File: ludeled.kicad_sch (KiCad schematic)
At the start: 2 parts

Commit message: Major layout and placement complete
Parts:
- removed SW1: (no value), symbol ludeled-rescue:SW_Push-Switch
- added JP1, JP2: SolderJumper_2_Open, Jumper:SolderJumper-2_P1.3mm_Open_TrianglePad1.0x1.5mm, symbol Jumper:SolderJumper_2_Open
- added JP3: SolderJumper_2_Open, Jumper:SolderJumper-2_P1.3mm_Bridged_RoundedPad1.0x1.5mm, symbol Jumper:SolderJumper_2_Bridged
- added SW1: SW_SPST, Button_Switch_SMD:SW_SPST_B3S-1000, symbol Switch:SW_SPST
- added U2: AMS1117-3.3, Package_TO_SOT_SMD:SOT-223-3_TabPin2, symbol Regulator_Linear:AMS1117-3.3
- U1: value (none) -> ESP32-WROOM-32E; footprint (none) -> RF_Module:ESP32-WROOM-32; symbol ludeled-rescue:ESP32-WROOM-32E-Espressif -> RF_Module:ESP32-WROOM-32
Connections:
- net FrontLeds/LED_LOWER_DIN: now also JP3.2 (B)
- new net: SW1.1 (A), U1.25 (IO0)
- new net: JP3.1 (A), U1.26 (IO4)
- new net +3.3V: JP2.2 (B), U1.2 (VDD)
- new net +5V: JP1.1 (A)
- new net 3V3_REG_IN_5V: JP1.2 (B), U2.3 (VI)
- new net 3V3_REG_OUT: JP2.1 (A), U2.2 (VO)
- new net GND: SW1.2 (B), U1.1 (GND), U1.15 (GND), U1.38 (GND), U1.39 (GND), U2.1 (GND)
- no-connect marks 0 -> 31

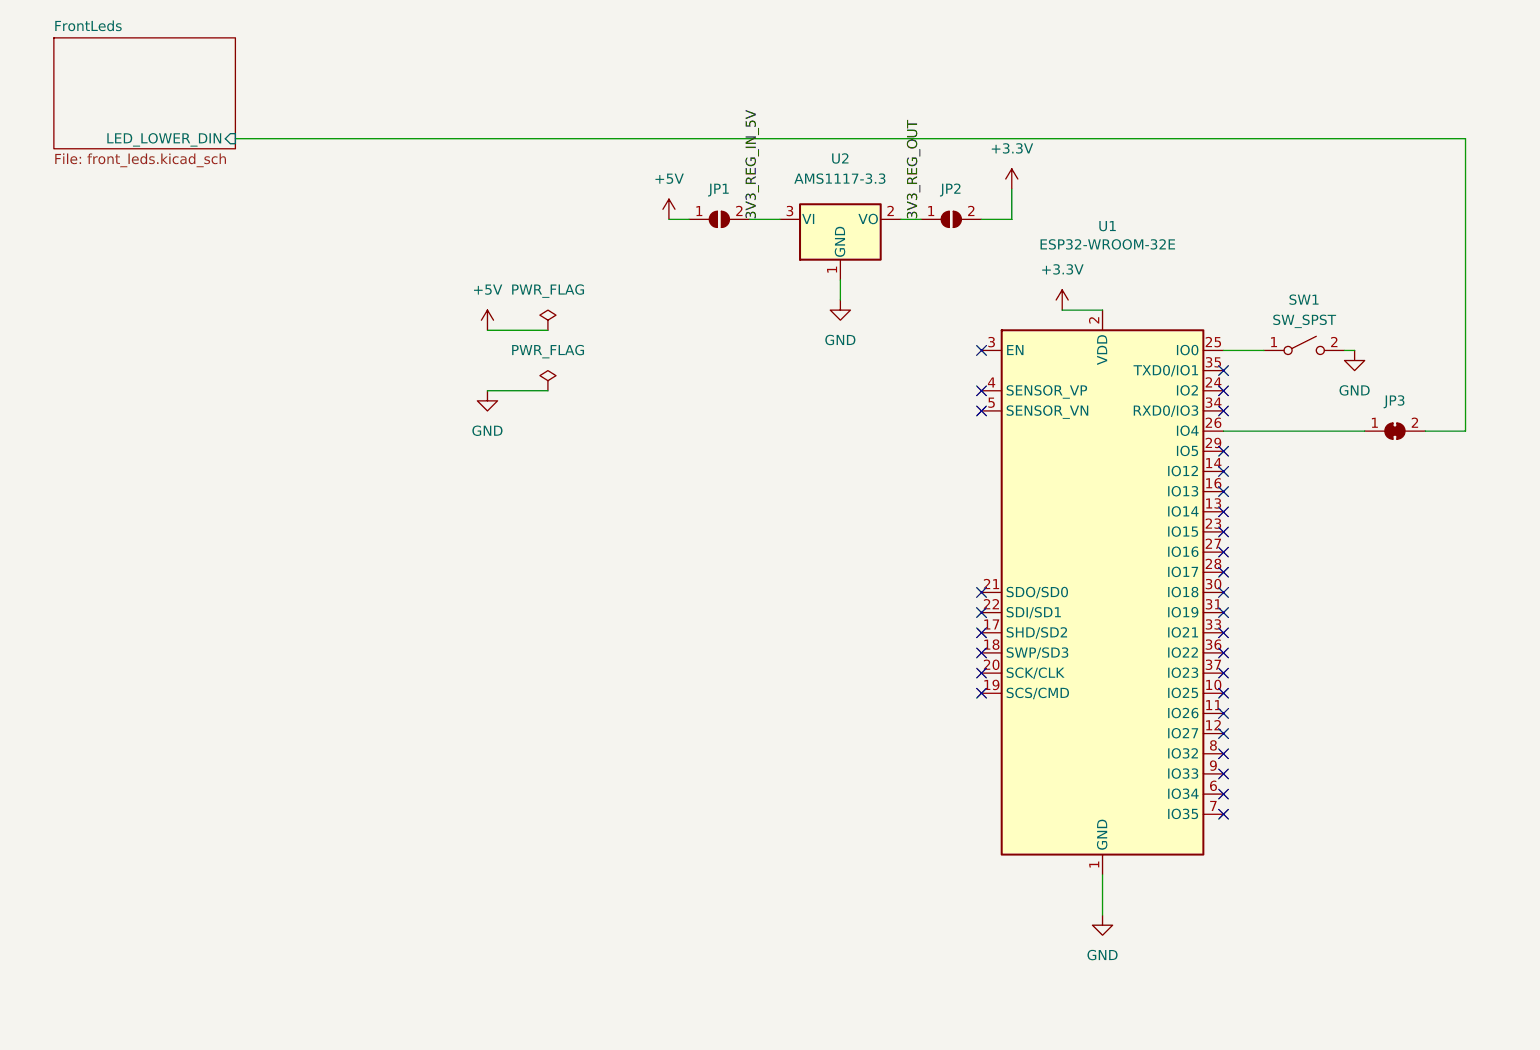
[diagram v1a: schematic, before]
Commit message: DRC fixes, cap footprint update, etc.
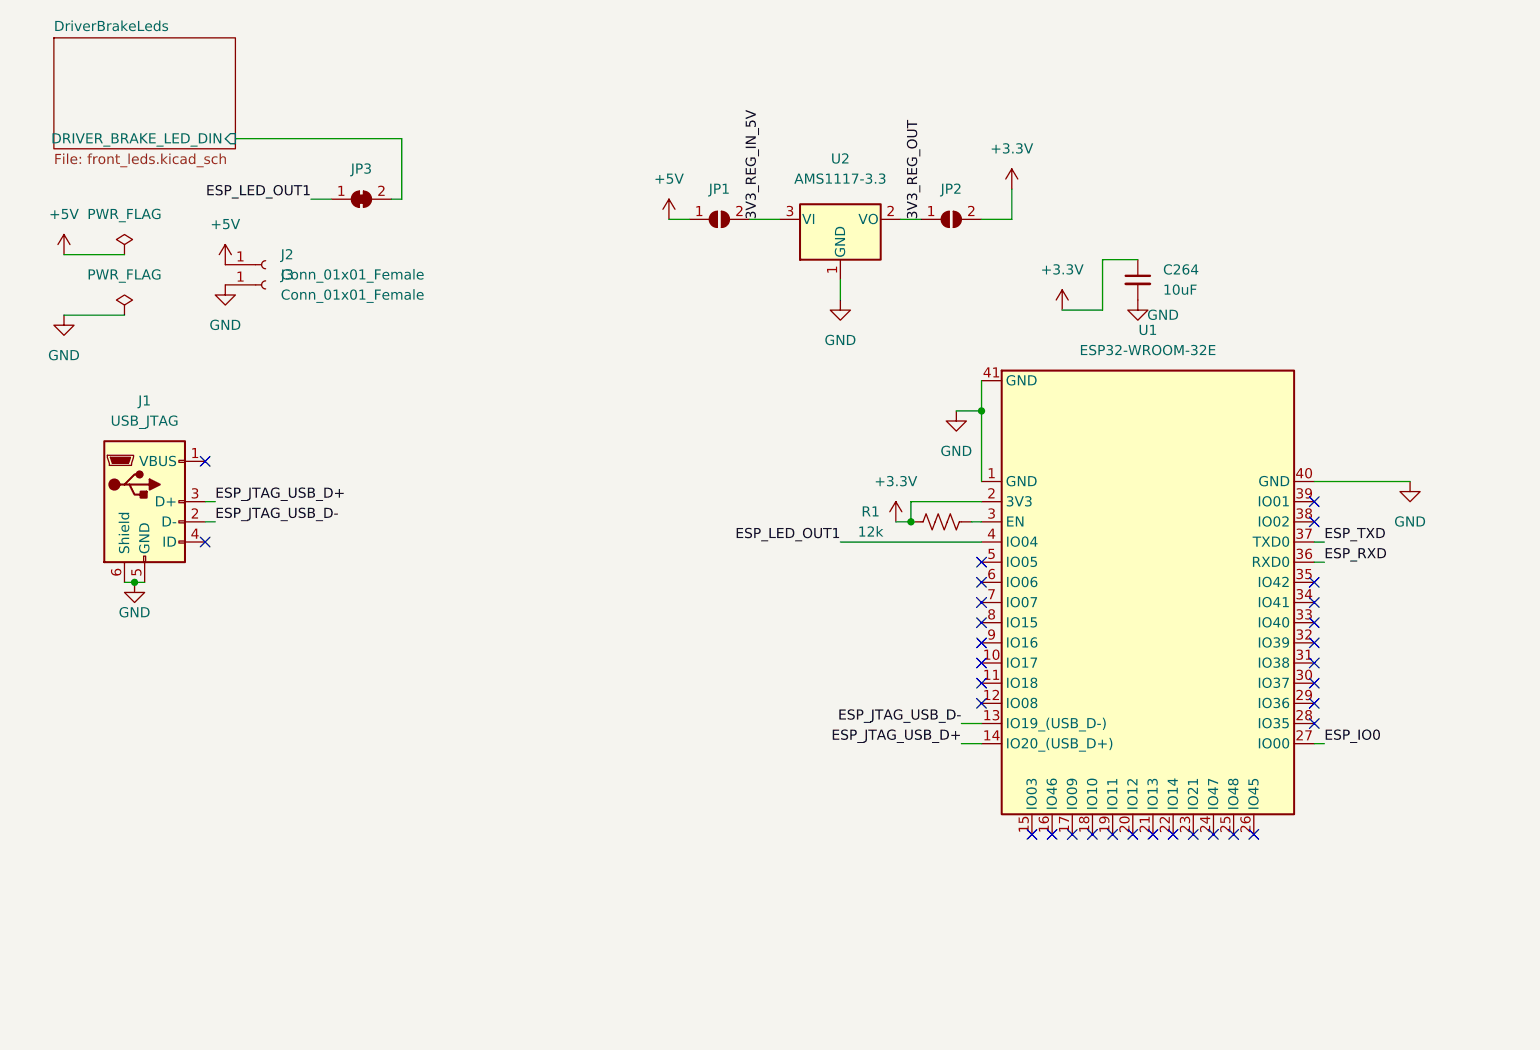
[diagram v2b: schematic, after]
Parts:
- removed SW1: SW_SPST, Button_Switch_SMD:SW_SPST_B3S-1000, symbol Switch:SW_SPST
- added C264: 10uF, Capacitor_SMD:C_0402_1005Metric, symbol Device:C_Small
- added J1: USB_JTAG, Connector_USB:USB_Micro-B_Molex_47346-0001, symbol Connector:USB_B_Micro
- added J2, J3: Conn_01x01_Female, Connector_Wire:SolderWirePad_1x01_SMD_5x10mm, symbol Connector:Conn_01x01_Female
- added R1: 12k, Resistor_SMD:R_0402_1005Metric, symbol Device:R_US
- U1: footprint RF_Module:ESP32-WROOM-32 -> RF_Module:ESP32-S3-WROOM-1; symbol RF_Module:ESP32-WROOM-32 -> ESP32:ESP32-S3-WROVER; now left out of the parts list
- U2: now left out of the parts list
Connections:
- net +3.3V: now also C264.1, R1.1
- net +5V: now also J2.1 (Pin_1)
- net GND: now also U1.40 (GND), U1.41 (GND), C264.2, J1.5 (GND), J1.6 (Shield), J3.1 (Pin_1); no longer U1.15 (GND), U1.38 (GND), U1.39 (GND)
- net ESP_JTAG_USB_D-: now reaches U1.13 (IO19_(USB_D-))
- net ESP_JTAG_USB_D-: now also J1.2 (D-)
- net ESP_JTAG_USB_D+: now reaches U1.14 (IO20_(USB_D+))
- net ESP_JTAG_USB_D+: now also J1.3 (D+)
- net at U1.26 (IO45): no longer JP3.1 (A)
- net ESP_IO0: now reaches U1.27 (IO00)
- net at U1.3 (EN): now also R1.2
- net ESP_RXD: now reaches U1.36 (RXD0)
- net ESP_TXD: now reaches U1.37 (TXD0)
- net ESP_LED_OUT1: now reaches U1.4 (IO04)
- net ESP_LED_OUT1: now also JP3.1 (A)
- net DriverBrakeLeds/LED_LOWER_DIN renamed DriverBrakeLeds/DRIVER_BRAKE_LED_DIN
- no-connect marks 31 -> 32
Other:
- sheet FrontLeds renamed DriverBrakeLeds
- sheet DriverBrakeLeds ports: added DRIVER_BRAKE_LED_DIN; removed LED_LOWER_DIN
- moved on the sheet: JP3
